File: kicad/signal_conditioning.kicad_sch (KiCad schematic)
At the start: 70 parts, among them U1A TL072, U1B TL072, U2A TL072, U2B TL072, U3A TL072, U3B TL072, U4A TL072, U4B TL072, U5A TL072, U5B TL072, U6A TL072, U6B TL072, U7A TL072, U7B TL072, U8A TL072

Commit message: kicad: Rev 3 schematic generator — strict 1.27mm grid alignment
All wire endpoints now verified on 1.27mm KiCad snap grid; labels placed
at exact pin/junction coordinates instead of 0.5mm stubs.  op-amp outputs
connect directly at y_rail with no off-grid intermediate points.

Co-Authored-By: Claude Sonnet 4.6 <noreply@anthropic.com>
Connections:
- net B2_CH0 is gone; now on net BUF2_CH0: U1B.7
- net B2_CH1 is gone; now on net BUF2_CH1: U3A.1
- net B2_CH2 is gone; now on net BUF2_CH2: U4B.7
- net B2_CH3 is gone; now on net BUF2_CH3: U6A.1
- net B2_CH4 is gone; now on net BUF2_CH4: U7B.7
- net ADS_CH0: now also U2A.2 (-); no longer C7.2
- net ADS_CH1: now also U3B.6 (-); no longer C18.2
- net ADS_CH2: now also U5A.2 (-); no longer C29.2
- net ADS_CH3: now also U6B.6 (-); no longer C40.2
- net ADS_CH4: now also U8A.2 (-); no longer C51.2
- net SK_A0: no longer C7.1
- net SK_A1: no longer C18.1
- net SK_A2: no longer C29.1
- net SK_A3: no longer C40.1
- net SK_A4: no longer C51.1
- net BUF2_CH3: now reaches U6A.2 (-)
- net DIV_CH3: now reaches U6A.3 (+)
- net DIV_CH2: now reaches U4B.5 (+)
- net BUF2_CH2: now reaches U4B.6 (-)
- net BUF1_CH0: now reaches U1A.1
- net BUF1_CH0: now also U1A.2 (-)
- net BUF1_CH1: now reaches U2B.6 (-)
- net BUF1_CH1: now also U2B.7
- net BUF1_CH4: now reaches U7A.1
- net BUF1_CH4: now also U7A.2 (-)
- net DIV_CH0: now reaches U1B.5 (+)
- net BUF2_CH0: now reaches U1B.6 (-)
- net BUF1_CH3: now reaches U5B.6 (-)
- net BUF1_CH3: now also U5B.7
- net DIV_CH4: now reaches U7B.5 (+)
- net BUF2_CH4: now reaches U7B.6 (-)
- net BUF2_CH1: now reaches U3A.2 (-)
- net DIV_CH1: now reaches U3A.3 (+)
- net BUF1_CH2: now reaches U4A.1
- net BUF1_CH2: now also U4A.2 (-)
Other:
- title: 5D Chaos Monitor — Signal Conditioning Front-End  (Rev 2) -> 5D Chaos Monitor — Signal Conditioning  Rev 3

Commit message: kicad: fix embedded lib_symbols outer names — add lib: prefix
Symbols embedded in lib_symbols must use "Device:R", "power:GND" etc.
to match the lib_id used in placements; bare "R", "GND" caused all
components to render as ? blocks.

Co-Authored-By: Claude Sonnet 4.6 <noreply@anthropic.com>
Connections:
- net ADS_CH0: now also C7.2, D10.2 (A), D11.1 (K)
- net ADS_CH1: now also C18.2, D21.2 (A), D22.1 (K)
- net ADS_CH2: now also C29.2, D32.2 (A), D33.1 (K)
- net ADS_CH3: now also C40.2, D43.2 (A), D44.1 (K)
- net ADS_CH4: now also C51.2, D54.2 (A), D55.1 (K)
- net BUF1_CH0: now also R4.1
- net BUF1_CH1: now also R15.1
- net BUF1_CH2: now also R26.1
- net BUF1_CH3: now also R37.1
- net BUF1_CH4: now also R48.1
- net BUF2_CH0: now also R6.1
- net BUF2_CH1: now also R17.1
- net BUF2_CH2: now also R28.1
- net BUF2_CH3: now also R39.1
- net BUF2_CH4: now also R50.1
- net CHUA_V: now also R45.1
- net CHUA_W: now also R34.1
- net CHUA_X: now also R1.1
- net CHUA_Y: now also R12.1
- net CHUA_Z: now also R23.1
- net DIV_CH0: now also R4.2, R5.1
- net DIV_CH1: now also R15.2, R16.1
- net DIV_CH2: now also R26.2, R27.1
- net DIV_CH3: now also R37.2, R38.1
- net DIV_CH4: now also R48.2, R49.1
- net SK_A0: now also C7.1, R6.2, R8.1
- net SK_A1: now also C18.1, R17.2, R19.1
- net SK_A2: now also C29.1, R28.2, R30.1
- net SK_A3: now also C40.1, R39.2, R41.1
- net SK_A4: now also C51.1, R50.2, R52.1
- net at U4A.3 (+): now also D24.2 (A), D25.1 (K), R23.2
- net at U5B.5 (+): now also D35.2 (A), D36.1 (K), R34.2
- net at U1A.3 (+): now also D2.2 (A), D3.1 (K), R1.2
- net at U3B.5 (+): now also C20.1, R19.2
- net at U5A.3 (+): now also C31.1, R30.2
- net at U2A.3 (+): now also C9.1, R8.2
- net at U8A.3 (+): now also C53.1, R52.2
- net at U6B.5 (+): now also C42.1, R41.2
- net at U2B.5 (+): now also D13.2 (A), D14.1 (K), R12.2
- net at U7A.3 (+): now also D46.2 (A), D47.1 (K), R45.2
- new net GND: C20.2, C31.2, C42.2, C53.2, C9.2, R16.2, R27.2, R38.2, R49.2, R5.2
- new net VCC: D10.1 (K), D13.1 (K), D2.1 (K), D21.1 (K), D24.1 (K), D32.1 (K), D35.1 (K), D43.1 (K), D46.1 (K), D54.1 (K)
- new net VEE: D11.2 (A), D14.2 (A), D22.2 (A), D25.2 (A), D3.2 (A), D33.2 (A), D36.2 (A), D44.2 (A), D47.2 (A), D55.2 (A)
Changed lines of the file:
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@@
   (symbol (lib_id "power:VCC") (at 27.9400 20.3200 0) (unit 1)
     (in_bom yes) (on_board yes) (dnp no)
-    (property "Reference" "#PWR_b04e" (at 27.94 22.32 0)
+    (property "Reference" "#PWR_e9bc" (at 27.94 22.32 0)
       (effects (font (size 1.27 1.27)) hide))
     (property "Value" "VCC" (at 27.94 18.32 0)
@@
   (symbol (lib_id "power:VEE") (at 27.9400 40.6400 0) (unit 1)
     (in_bom yes) (on_board yes) (dnp no)
-    (property "Reference" "#PWR_7b68" (at 27.94 42.64 0)
+    (property "Reference" "#PWR_8d1d" (at 27.94 42.64 0)
       (effects (font (size 1.27 1.27)) hide))
     (property "Value" "VEE" (at 27.94 38.64 0)
@@
   (symbol (lib_id "power:GND") (at 57.1500 40.6400 270) (unit 1)
     (in_bom yes) (on_board yes) (dnp no)
-    (property "Reference" "#PWR_eb0b" (at 57.15 42.64 0)
+    (property "Reference" "#PWR_1e55" (at 57.15 42.64 0)
       (effects (font (size 1.27 1.27)) hide))
     (property "Value" "GND" (at 57.15 38.64 0)
@@
   (symbol (lib_id "power:GND") (at 107.9500 43.1800 270) (unit 1)
     (in_bom yes) (on_board yes) (dnp no)
-    (property "Reference" "#PWR_d3a8" (at 107.95 45.18 0)
+    (property "Reference" "#PWR_8a30" (at 107.95 45.18 0)
       (effects (font (size 1.27 1.27)) hide))
     (property "Value" "GND" (at 107.95 41.18 0)
@@
   (symbol (lib_id "power:VCC") (at 139.7000 20.3200 0) (unit 1)
     (in_bom yes) (on_board yes) (dnp no)
-    (property "Reference" "#PWR_013a" (at 139.70 22.32 0)
+    (property "Reference" "#PWR_c53a" (at 139.70 22.32 0)
       (effects (font (size 1.27 1.27)) hide))
     (property "Value" "VCC" (at 139.70 18.32 0)
@@
   (symbol (lib_id "power:VEE") (at 139.7000 40.6400 0) (unit 1)
     (in_bom yes) (on_board yes) (dnp no)
-    (property "Reference" "#PWR_cbfe" (at 139.70 42.64 0)
+    (property "Reference" "#PWR_4694" (at 139.70 42.64 0)
       (effects (font (size 1.27 1.27)) hide))
     (property "Value" "VEE" (at 139.70 38.64 0)
@@
   (symbol (lib_id "power:VCC") (at 27.9400 81.2800 0) (unit 1)
     (in_bom yes) (on_board yes) (dnp no)
-    (property "Reference" "#PWR_fec8" (at 27.94 83.28 0)
+    (property "Reference" "#PWR_4266" (at 27.94 83.28 0)
       (effects (font (size 1.27 1.27)) hide))
     (property "Value" "VCC" (at 27.94 79.28 0)
@@
   (symbol (lib_id "power:VEE") (at 27.9400 101.6000 0) (unit 1)
     (in_bom yes) (on_board yes) (dnp no)
-    (property "Reference" "#PWR_1702" (at 27.94 103.60 0)
+    (property "Reference" "#PWR_43f0" (at 27.94 103.60 0)
       (effects (font (size 1.27 1.27)) hide))
     (property "Value" "VEE" (at 27.94 99.60 0)
@@
   (symbol (lib_id "power:GND") (at 57.1500 101.6000 270) (unit 1)
     (in_bom yes) (on_board yes) (dnp no)
-    (property "Reference" "#PWR_70db" (at 57.15 103.60 0)
+    (property "Reference" "#PWR_8d7e" (at 57.15 103.60 0)
       (effects (font (size 1.27 1.27)) hide))
     (property "Value" "GND" (at 57.15 99.60 0)
@@
   (symbol (lib_id "power:GND") (at 107.9500 104.1400 270) (unit 1)
     (in_bom yes) (on_board yes) (dnp no)
-    (property "Reference" "#PWR_b3b6" (at 107.95 106.14 0)
+    (property "Reference" "#PWR_f35a" (at 107.95 106.14 0)
       (effects (font (size 1.27 1.27)) hide))
     (property "Value" "GND" (at 107.95 102.14 0)
@@
   (symbol (lib_id "power:VCC") (at 139.7000 81.2800 0) (unit 1)
     (in_bom yes) (on_board yes) (dnp no)
-    (property "Reference" "#PWR_a071" (at 139.70 83.28 0)
+    (property "Reference" "#PWR_229d" (at 139.70 83.28 0)
       (effects (font (size 1.27 1.27)) hide))
     (property "Value" "VCC" (at 139.70 79.28 0)
@@
   (symbol (lib_id "power:VEE") (at 139.7000 101.6000 0) (unit 1)
     (in_bom yes) (on_board yes) (dnp no)
-    (property "Reference" "#PWR_22cb" (at 139.70 103.60 0)
+    (property "Reference" "#PWR_fd3e" (at 139.70 103.60 0)
       (effects (font (size 1.27 1.27)) hide))
     (property "Value" "VEE" (at 139.70 99.60 0)
@@
   (symbol (lib_id "power:VCC") (at 27.9400 142.2400 0) (unit 1)
     (in_bom yes) (on_board yes) (dnp no)
-    (property "Reference" "#PWR_d319" (at 27.94 144.24 0)
+    (property "Reference" "#PWR_68a9" (at 27.94 144.24 0)
       (effects (font (size 1.27 1.27)) hide))
     (property "Value" "VCC" (at 27.94 140.24 0)
@@
   (symbol (lib_id "power:VEE") (at 27.9400 162.5600 0) (unit 1)
     (in_bom yes) (on_board yes) (dnp no)
-    (property "Reference" "#PWR_7978" (at 27.94 164.56 0)
+    (property "Reference" "#PWR_19b9" (at 27.94 164.56 0)
       (effects (font (size 1.27 1.27)) hide))
     (property "Value" "VEE" (at 27.94 160.56 0)
@@
   (symbol (lib_id "power:GND") (at 57.1500 162.5600 270) (unit 1)
     (in_bom yes) (on_board yes) (dnp no)
-    (property "Reference" "#PWR_18c6" (at 57.15 164.56 0)
+    (property "Reference" "#PWR_df2d" (at 57.15 164.56 0)
       (effects (font (size 1.27 1.27)) hide))
     (property "Value" "GND" (at 57.15 160.56 0)
@@
   (symbol (lib_id "power:GND") (at 107.9500 165.1000 270) (unit 1)
     (in_bom yes) (on_board yes) (dnp no)
-    (property "Reference" "#PWR_06d4" (at 107.95 167.10 0)
+    (property "Reference" "#PWR_2a01" (at 107.95 167.10 0)
       (effects (font (size 1.27 1.27)) hide))
     (property "Value" "GND" (at 107.95 163.10 0)
@@
   (symbol (lib_id "power:VCC") (at 139.7000 142.2400 0) (unit 1)
     (in_bom yes) (on_board yes) (dnp no)
-    (property "Reference" "#PWR_7820" (at 139.70 144.24 0)
+    (property "Reference" "#PWR_cdb6" (at 139.70 144.24 0)
       (effects (font (size 1.27 1.27)) hide))
     (property "Value" "VCC" (at 139.70 140.24 0)
@@
   (symbol (lib_id "power:VEE") (at 139.7000 162.5600 0) (unit 1)
     (in_bom yes) (on_board yes) (dnp no)
-    (property "Reference" "#PWR_3381" (at 139.70 164.56 0)
+    (property "Reference" "#PWR_cdc5" (at 139.70 164.56 0)
       (effects (font (size 1.27 1.27)) hide))
     (property "Value" "VEE" (at 139.70 160.56 0)
@@
   (symbol (lib_id "power:VCC") (at 27.9400 203.2000 0) (unit 1)
     (in_bom yes) (on_board yes) (dnp no)
-    (property "Reference" "#PWR_053f" (at 27.94 205.20 0)
+    (property "Reference" "#PWR_899e" (at 27.94 205.20 0)
       (effects (font (size 1.27 1.27)) hide))
     (property "Value" "VCC" (at 27.94 201.20 0)
@@
   (symbol (lib_id "power:VEE") (at 27.9400 223.5200 0) (unit 1)
     (in_bom yes) (on_board yes) (dnp no)
-    (property "Reference" "#PWR_f8cb" (at 27.94 225.52 0)
+    (property "Reference" "#PWR_7265" (at 27.94 225.52 0)
       (effects (font (size 1.27 1.27)) hide))
     (property "Value" "VEE" (at 27.94 221.52 0)
@@
   (symbol (lib_id "power:GND") (at 57.1500 223.5200 270) (unit 1)
     (in_bom yes) (on_board yes) (dnp no)
-    (property "Reference" "#PWR_12e8" (at 57.15 225.52 0)
+    (property "Reference" "#PWR_4ab3" (at 57.15 225.52 0)
       (effects (font (size 1.27 1.27)) hide))
     (property "Value" "GND" (at 57.15 221.52 0)
@@
   (symbol (lib_id "power:GND") (at 107.9500 226.0600 270) (unit 1)
     (in_bom yes) (on_board yes) (dnp no)
-    (property "Reference" "#PWR_85d2" (at 107.95 228.06 0)
+    (property "Reference" "#PWR_856d" (at 107.95 228.06 0)
       (effects (font (size 1.27 1.27)) hide))
     (property "Value" "GND" (at 107.95 224.06 0)
@@
   (symbol (lib_id "power:VCC") (at 139.7000 203.2000 0) (unit 1)
     (in_bom yes) (on_board yes) (dnp no)
-    (property "Reference" "#PWR_3065" (at 139.70 205.20 0)
+    (property "Reference" "#PWR_7490" (at 139.70 205.20 0)
       (effects (font (size 1.27 1.27)) hide))
     (property "Value" "VCC" (at 139.70 201.20 0)
@@
   (symbol (lib_id "power:VEE") (at 139.7000 223.5200 0) (unit 1)
     (in_bom yes) (on_board yes) (dnp no)
-    (property "Reference" "#PWR_3189" (at 139.70 225.52 0)
+    (property "Reference" "#PWR_2e4b" (at 139.70 225.52 0)
       (effects (font (size 1.27 1.27)) hide))
     (property "Value" "VEE" (at 139.70 221.52 0)
@@
   (symbol (lib_id "power:VCC") (at 27.9400 264.1600 0) (unit 1)
     (in_bom yes) (on_board yes) (dnp no)
-    (property "Reference" "#PWR_4b9e" (at 27.94 266.16 0)
+    (property "Reference" "#PWR_c5d0" (at 27.94 266.16 0)
       (effects (font (size 1.27 1.27)) hide))
     (property "Value" "VCC" (at 27.94 262.16 0)
@@
   (symbol (lib_id "power:VEE") (at 27.9400 284.4800 0) (unit 1)
     (in_bom yes) (on_board yes) (dnp no)
-    (property "Reference" "#PWR_49cc" (at 27.94 286.48 0)
+    (property "Reference" "#PWR_34c4" (at 27.94 286.48 0)
       (effects (font (size 1.27 1.27)) hide))
     (property "Value" "VEE" (at 27.94 282.48 0)
@@
   (symbol (lib_id "power:GND") (at 57.1500 284.4800 270) (unit 1)
     (in_bom yes) (on_board yes) (dnp no)
-    (property "Reference" "#PWR_c21a" (at 57.15 286.48 0)
+    (property "Reference" "#PWR_1cde" (at 57.15 286.48 0)
       (effects (font (size 1.27 1.27)) hide))
     (property "Value" "GND" (at 57.15 282.48 0)
@@
   (symbol (lib_id "power:GND") (at 107.9500 287.0200 270) (unit 1)
     (in_bom yes) (on_board yes) (dnp no)
-    (property "Reference" "#PWR_d026" (at 107.95 289.02 0)
+    (property "Reference" "#PWR_8465" (at 107.95 289.02 0)
       (effects (font (size 1.27 1.27)) hide))
     (property "Value" "GND" (at 107.95 285.02 0)
@@
   (symbol (lib_id "power:VCC") (at 139.7000 264.1600 0) (unit 1)
     (in_bom yes) (on_board yes) (dnp no)
-    (property "Reference" "#PWR_cce7" (at 139.70 266.16 0)
+    (property "Reference" "#PWR_a8d1" (at 139.70 266.16 0)
       (effects (font (size 1.27 1.27)) hide))
     (property "Value" "VCC" (at 139.70 262.16 0)
@@
   (symbol (lib_id "power:VEE") (at 139.7000 284.4800 0) (unit 1)
     (in_bom yes) (on_board yes) (dnp no)
-    (property "Reference" "#PWR_52a1" (at 139.70 286.48 0)
+    (property "Reference" "#PWR_af7c" (at 139.70 286.48 0)
       (effects (font (size 1.27 1.27)) hide))
     (property "Value" "VEE" (at 139.70 282.48 0)

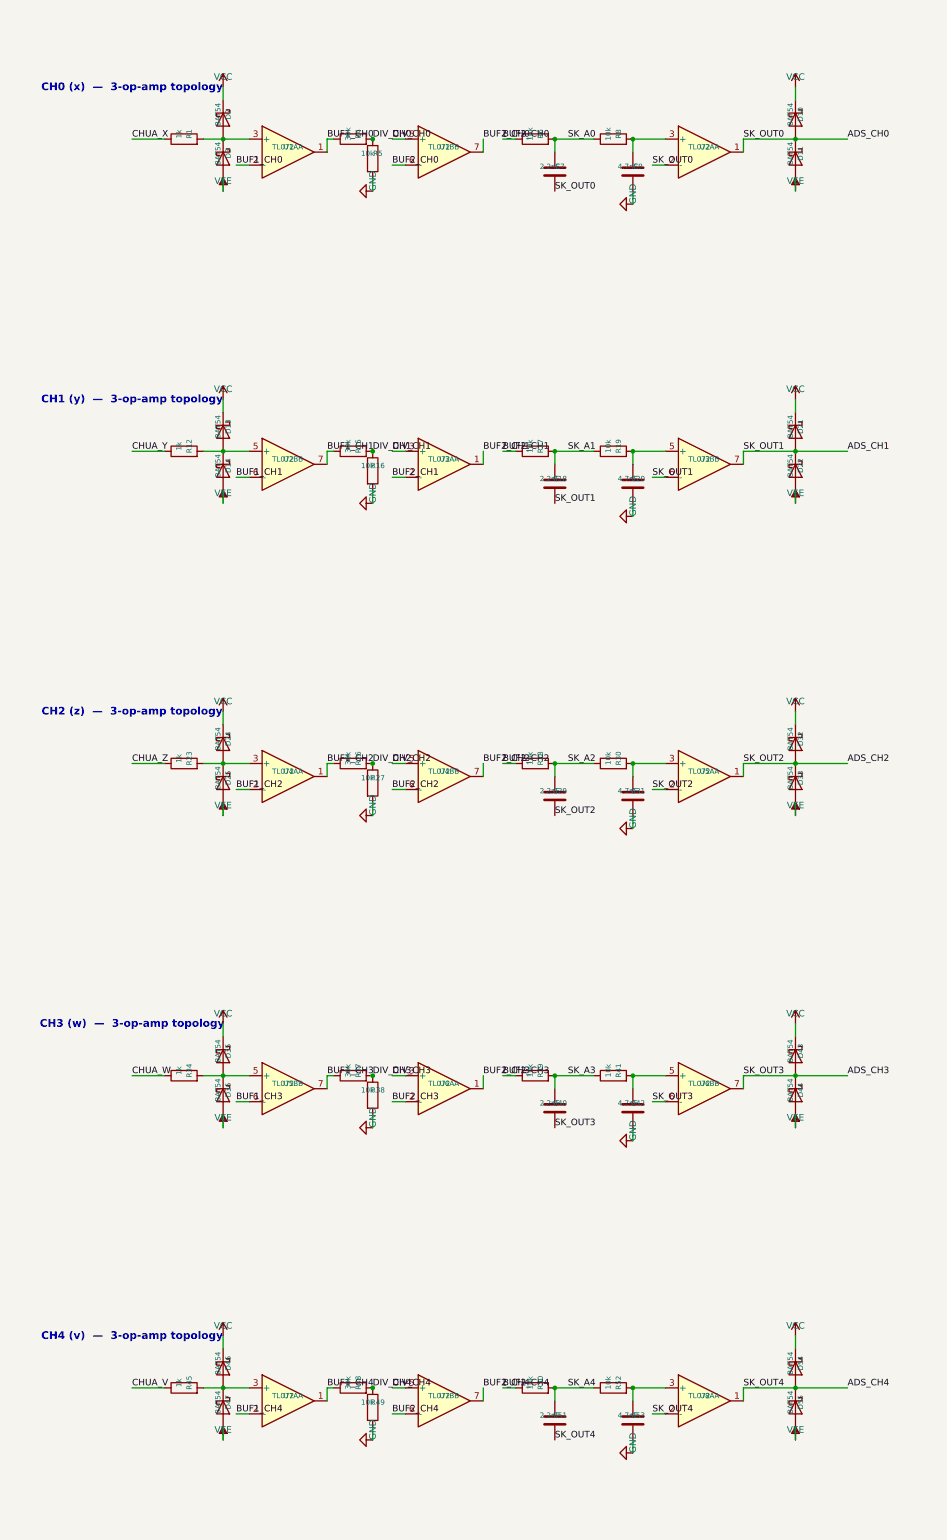
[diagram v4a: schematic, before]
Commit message: kicad: push hand-edited schematic with full routing
KiCad-edited version: VEE symbols mirrored, GND corrected, unity-gain
feedback wires routed, labels repositioned above signal rail.

Co-Authored-By: Claude Sonnet 4.6 <noreply@anthropic.com>
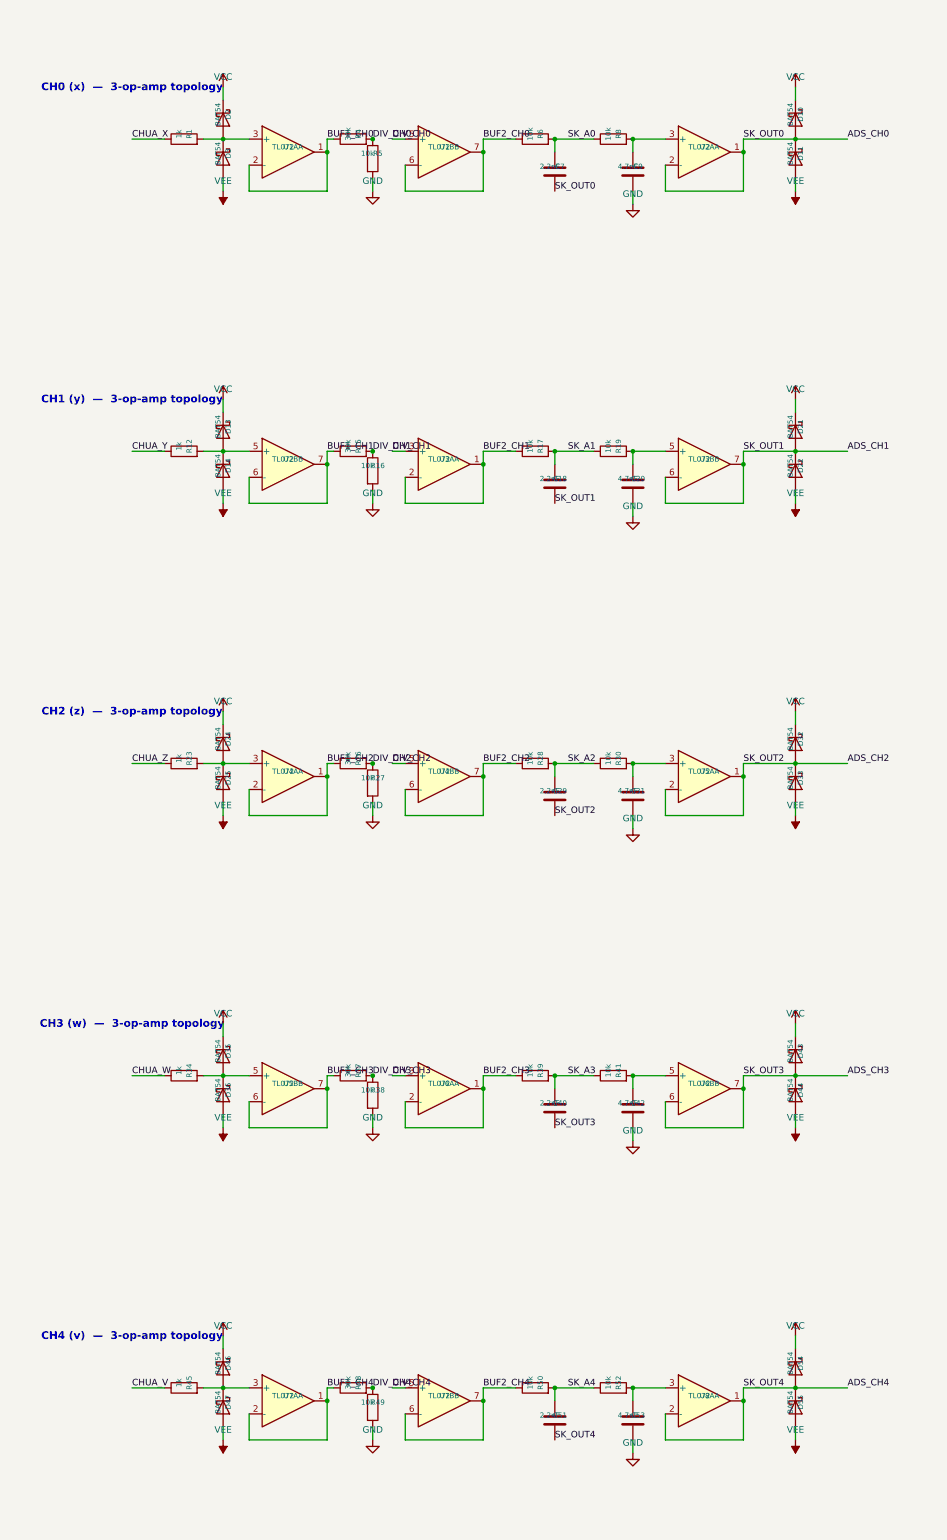
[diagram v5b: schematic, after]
